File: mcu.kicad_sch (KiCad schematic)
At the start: 38 parts, among them J2 RJ45_Shielded, J4 Micro_SD_Card_Det1, J6 Conn_01x03_Pin, J7 RFShield_TwoPieces, SW1 SW_Push, SW2 SW_Push, SW3 SW_Push, SW4 SW_Push, U1 nRF54L15-QFXX, U9 TPD6F003, Y1 32MHz, Y2 32.768KHz

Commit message: mark NFC components as DNP for rev1
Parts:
- AE1, C15, C16, C17, C18: now not fitted
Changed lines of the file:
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@@
 		(in_bom yes)
 		(on_board yes)
-		(dnp no)
+		(dnp yes)
 		(fields_autoplaced yes)
 		(property "Reference" "C16"
@@
 		(in_bom yes)
 		(on_board yes)
-		(dnp no)
+		(dnp yes)
 		(fields_autoplaced yes)
 		(property "Reference" "C17"
@@
 		(in_bom yes)
 		(on_board yes)
-		(dnp no)
+		(dnp yes)
 		(fields_autoplaced yes)
 		(property "Reference" "C18"
@@
 		(in_bom yes)
 		(on_board yes)
-		(dnp no)
+		(dnp yes)
 		(fields_autoplaced yes)
 		(property "Reference" "AE1"
@@
 		(in_bom yes)
 		(on_board yes)
-		(dnp no)
+		(dnp yes)
 		(fields_autoplaced yes)
 		(property "Reference" "C15"

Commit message: clarify and set up board stackup properly
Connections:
- net 1.8V: now also U1.30 (~{RESET})
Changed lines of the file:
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@@
 		(shape output)
 		(at 124.46 116.84 180)
+		(fields_autoplaced yes)
 		(effects
 			(font
@@
 		(shape passive)
 		(at 39.37 41.91 0)
+		(fields_autoplaced yes)
 		(effects
 			(font
@@
 		(shape output)
 		(at 124.46 133.35 180)
+		(fields_autoplaced yes)
 		(effects
 			(font
@@
 		(shape output)
 		(at 173.99 148.59 180)
+		(fields_autoplaced yes)
 		(effects
 			(font
@@
 		(shape bidirectional)
 		(at 124.46 111.76 180)
+		(fields_autoplaced yes)
 		(effects
 			(font
@@
 		(shape passive)
 		(at 69.85 172.72 0)
+		(fields_autoplaced yes)
 		(effects
 			(font
@@
 		(shape bidirectional)
 		(at 124.46 128.27 180)
+		(fields_autoplaced yes)
 		(effects
 			(font
@@
 		(shape input)
 		(at 170.18 143.51 180)
+		(fields_autoplaced yes)
 		(effects
 			(font
@@
 		(shape output)
 		(at 171.45 118.11 180)
+		(fields_autoplaced yes)
 		(effects
 			(font
@@
 		)
 	)
+	(hierarchical_label "1.8V"
+		(shape input)
+		(at 232.41 143.51 0)
+		(fields_autoplaced yes)
+		(effects
+			(font
+				(size 1.27 1.27)
+			)
+			(justify left)
+		)
+	)
 	(hierarchical_label "SCLK"
 		(shape output)
 		(at 173.99 140.97 180)
+		(fields_autoplaced yes)
 		(effects
 			(font
@@
 		(shape output)
 		(at 173.99 146.05 180)
+		(fields_autoplaced yes)
 		(effects
 			(font
@@
 		(shape input)
 		(at 171.45 120.65 180)
+		(fields_autoplaced yes)
 		(effects
 			(font
@@
 		(shape passive)
 		(at 125.73 106.68 180)
+		(fields_autoplaced yes)
 		(effects
 			(font
@@
 		(shape passive)
 		(at 125.73 123.19 180)
+		(fields_autoplaced yes)
 		(effects
 			(font
@@
 		(shape input)
 		(at 144.78 30.48 90)
+		(fields_autoplaced yes)
 		(effects
 			(font

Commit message: shitty routing job for rev1
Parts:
- C22, C23, C24, C25, C26: footprint (none) -> Capacitor_SMD:C_0201_0603Metric
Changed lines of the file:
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@@
 			)
 		)
-		(property "Footprint" ""
+		(property "Footprint" "Capacitor_SMD:C_0201_0603Metric"
 			(at 181.61 35.56 0)
 			(effects
@@
 			)
 		)
-		(property "Footprint" ""
+		(property "Footprint" "Capacitor_SMD:C_0201_0603Metric"
 			(at 170.18 35.56 0)
 			(effects
@@
 			)
 		)
-		(property "Footprint" ""
+		(property "Footprint" "Capacitor_SMD:C_0201_0603Metric"
 			(at 157.48 35.56 0)
 			(effects
@@
 		(exclude_from_sim no)
 		(in_bom yes)
-		(on_board yes)
-		(dnp no)
+		(on_board no)
+		(dnp yes)
 		(fields_autoplaced yes)
 		(property "Reference" "#PWR017"
@@
 		(exclude_from_sim no)
 		(in_bom yes)
-		(on_board yes)
-		(dnp no)
+		(on_board no)
+		(dnp yes)
 		(fields_autoplaced yes)
 		(property "Reference" "#PWR018"
@@
 		(exclude_from_sim no)
 		(in_bom yes)
-		(on_board yes)
-		(dnp no)
+		(on_board no)
+		(dnp yes)
 		(property "Reference" "#PWR019"
 			(at 140.97 78.74 0)
@@
 		(exclude_from_sim no)
 		(in_bom yes)
-		(on_board yes)
-		(dnp no)
+		(on_board no)
+		(dnp yes)
 		(property "Reference" "#PWR020"
 			(at 153.67 78.74 0)
@@
 			)
 		)
-		(property "Footprint" ""
+		(property "Footprint" "Capacitor_SMD:C_0201_0603Metric"
 			(at 194.31 35.56 0)
 			(effects
@@
 			)
 		)
-		(property "Footprint" ""
+		(property "Footprint" "Capacitor_SMD:C_0201_0603Metric"
 			(at 144.78 35.56 0)
 			(effects

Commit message: change RF shield
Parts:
- J7: footprint RF_Shielding:Laird_Technologies_BMI-S-103_26.21x26.21mm -> RF_Shielding:Wuerth_36103205_20x20mm
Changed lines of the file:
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@@
 			)
 		)
-		(property "Footprint" "RF_Shielding:Laird_Technologies_BMI-S-103_26.21x26.21mm"
+		(property "Footprint" "RF_Shielding:Wuerth_36103205_20x20mm"
 			(at 85.09 57.15 0)
 			(effects

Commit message: begin new board
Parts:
- SW1, SW2, SW3, SW4: footprint (none) -> Button_Switch_SMD:SW_SPST_PTS647_Sx50
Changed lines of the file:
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@@
 			)
 		)
-		(property "Footprint" ""
+		(property "Footprint" "Button_Switch_SMD:SW_SPST_PTS647_Sx50"
 			(at 29.21 133.35 0)
 			(effects
@@
 			)
 		)
-		(property "Footprint" ""
+		(property "Footprint" "Button_Switch_SMD:SW_SPST_PTS647_Sx50"
 			(at 29.21 121.92 0)
 			(effects
@@
 			)
 		)
-		(property "Footprint" ""
+		(property "Footprint" "Button_Switch_SMD:SW_SPST_PTS647_Sx50"
 			(at 29.21 110.49 0)
 			(effects
@@
 			)
 		)
-		(property "Footprint" ""
+		(property "Footprint" "Button_Switch_SMD:SW_SPST_PTS647_Sx50"
 			(at 29.21 99.06 0)
 			(effects

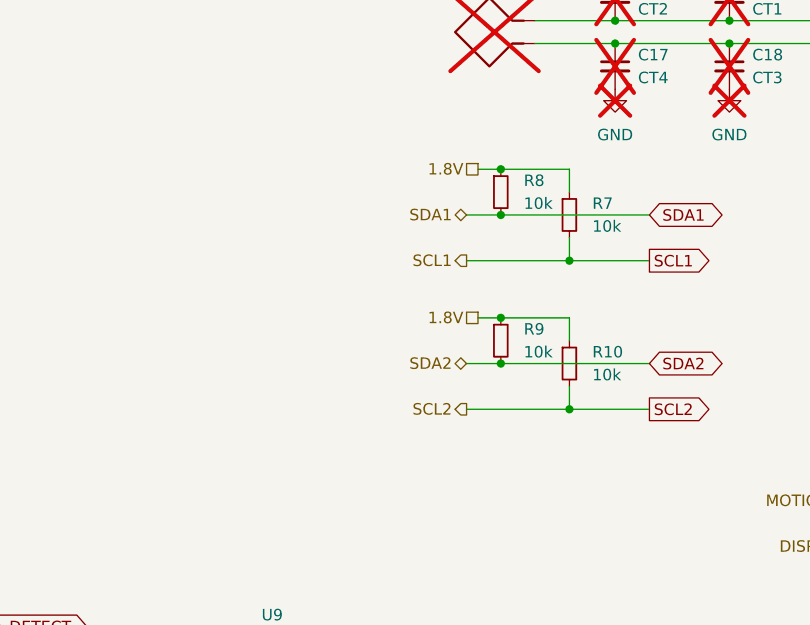
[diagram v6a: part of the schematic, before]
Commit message: add lots of test points
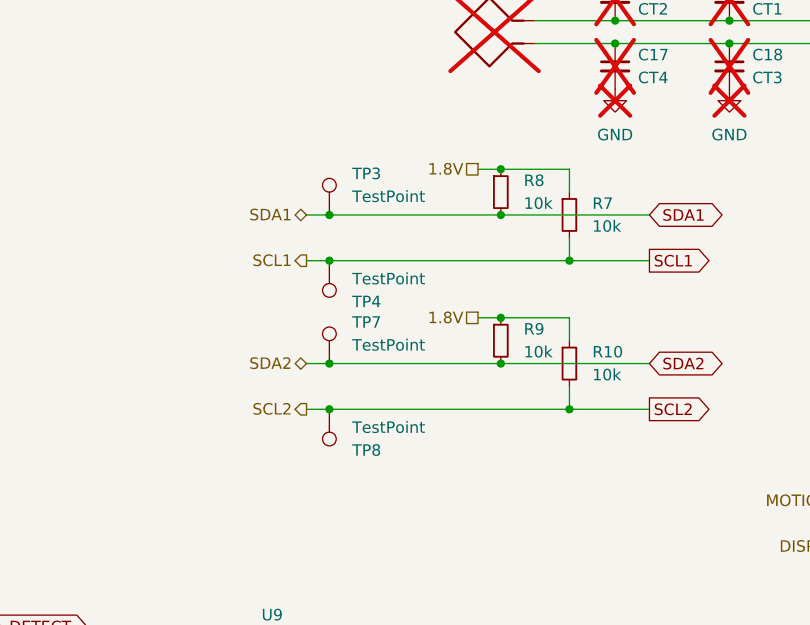
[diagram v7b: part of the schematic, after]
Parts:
- added TP3, TP4, TP7, TP8: TestPoint, symbol Connector:TestPoint
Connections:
- net SCL1: now also TP4.1
- net SCL2: now also TP8.1
- net SDA1: now also TP3.1
- net SDA2: now also TP7.1

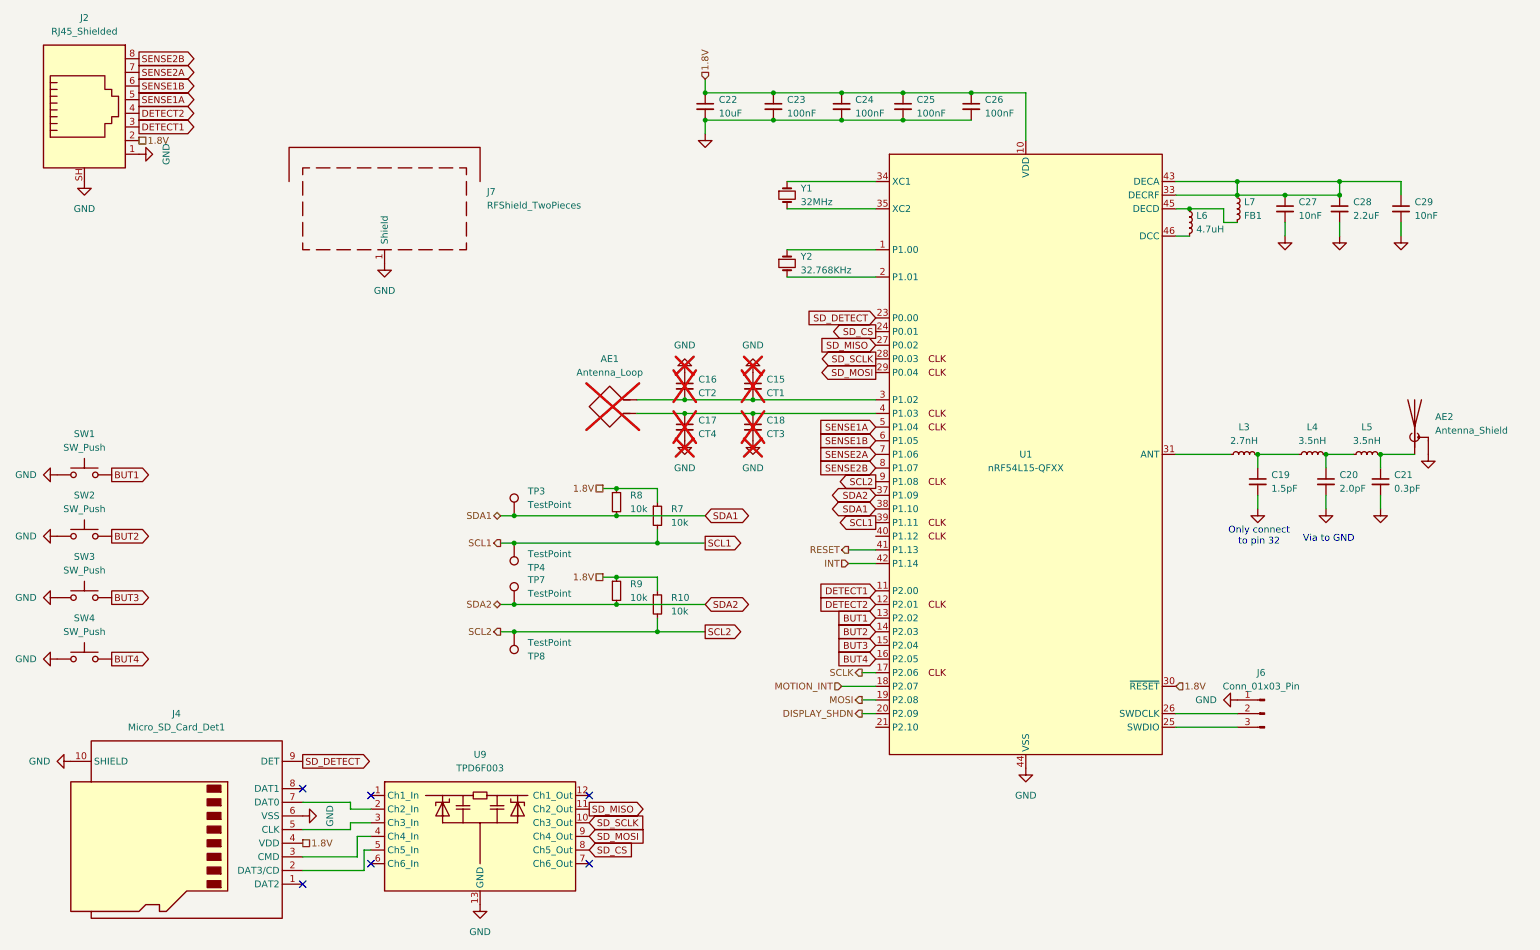
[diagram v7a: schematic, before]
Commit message: route PMIC
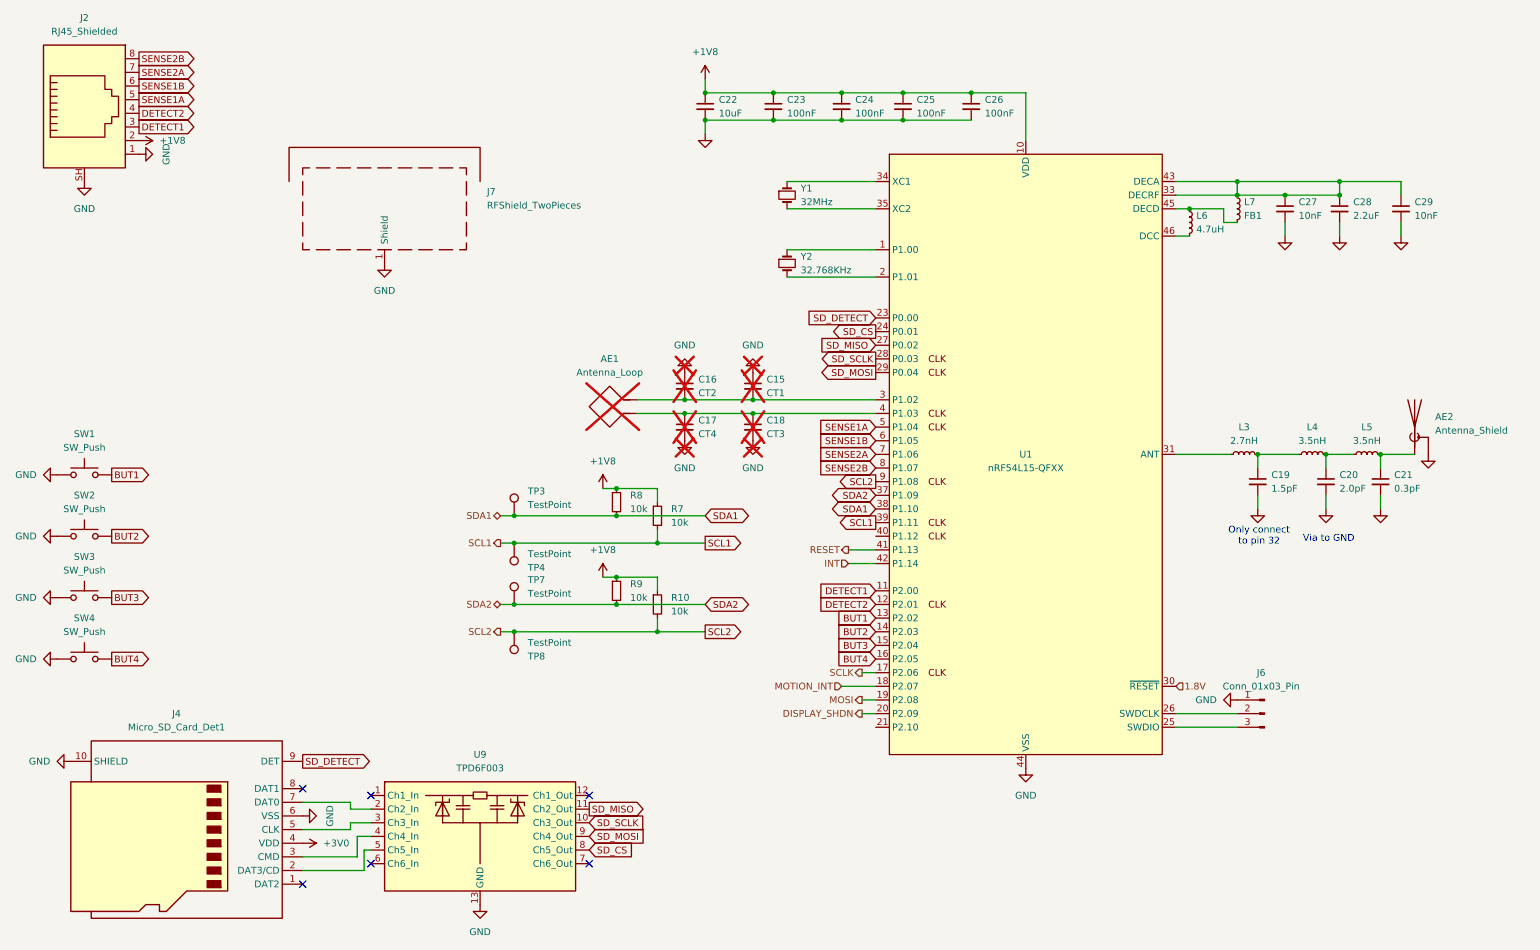
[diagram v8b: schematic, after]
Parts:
- TP3, TP4: footprint (none) -> TestPoint:TestPoint_Pad_1.0x1.0mm
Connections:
- net 1.8V: no longer C22.1, C23.1, C24.1, C25.1, C26.1, J2.2, J4.4 (VDD), R10.1, R7.1, R8.1, R9.1, U1.10 (VDD), U1.22 (VDD), U1.36 (VDD), U1.47 (VDD), U1.48 (VDD)
- new net +1V8: C22.1, C23.1, C24.1, C25.1, C26.1, J2.2, R10.1, R7.1, R8.1, R9.1, U1.10 (VDD), U1.22 (VDD), U1.36 (VDD), U1.47 (VDD), U1.48 (VDD)
- new net +3V0: J4.4 (VDD)
